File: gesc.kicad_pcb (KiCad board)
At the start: 4 copper layers, 111 x 111 mm, 150 parts, among them J1 Conn_01x06, J10 PHASE_C, J11 PHASE_B, J12 NTC, J13 T-Motor, J14 Conn_01x03, J15 EXT_OFF, J2 Conn_01x06, J3 Conn_01x06, J4 Conn_01x05, J5 Conn_01x03, J6 USB_B_Mini, J7 BAT+, J8 BAT-, J9 PHASE_A, Q1 TPH2R608NH,L1Q, Q2 TPH2R608NH,L1Q, Q3 TPH2R608NH,L1Q, Q4 TPH2R608NH,L1Q, Q5 TPH2R608NH,L1Q, Q6 TPH2R608NH,L1Q, U1 STM32F405RGTx, U10 LM5008MM, U11 SN74LVC1G66DBVR, U12 LM5107, U13 SN74LVC1G66DBVR, U14 TPS5430DDA, U15 LM5107, U16 EYSGJNZWY, U18 AQY282S, U2 SN74LVC1G66DBVR, U3 LM5107, U4 INA240A2, U5 INA240A2, U6 INA240A2, U7 SN74LVC1G66DBVR, U8 SN74LVC1G66DBVR, U9 SN74LVC1G66DBVR, Y1 X50328MSB2GI

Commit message: save
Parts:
- removed D10, D9: SMMBD914LT3G, Package_TO_SOT_SMD:SOT-23
- removed U18: AQY282S, Package_SO:SO-4_4.4x4.3mm_P2.54mm
- added C50: 22u/25V, Capacitor_SMD:C_0805_2012Metric, F.Cu at (175.5, 30.6)
- added C51: 10u0/75V, Capacitor_SMD:C_1210_3225Metric, F.Cu at (149.3, 31.2)
- added C52: 10u0/75V, Capacitor_SMD:C_1210_3225Metric, F.Cu at (149.3, 35.4)
- added C53: 10u0/75V, Capacitor_SMD:C_1210_3225Metric, F.Cu at (154.9, 31.2)
- added C55: 10u0/75V, Capacitor_SMD:C_1210_3225Metric, F.Cu at (154.9, 35.4)
- added C57: 10u0/75V, Capacitor_SMD:C_1210_3225Metric, F.Cu at (160.5, 31.2)
- added C58: 10u0/75V, Capacitor_SMD:C_1210_3225Metric, F.Cu at (160.5, 35.4)
- added D7: PMLL4153, Diode_SMD:D_MiniMELF, F.Cu at (170.1, 30.7)
- added R44: 34k0, Resistor_SMD:R_0805_2012Metric, F.Cu at (174.9, 33.8)
- added U17: LMR12010YMKE_NOPB, gesc:SOT95P280X110-6N, F.Cu at (88.0, 161.5)
- C19: value 100n -> 1u00
- C20, C31: value 10n0 -> 100n
- C23: value 10n0 -> 2n20
- C28: value 10u0/25V -> 22u/25V
- C33: value 100u -> 100n; footprint Capacitor_Tantalum_SMD:CP_EIA-3528-21_Kemet-B -> Capacitor_SMD:C_0805_2012Metric
- C34: value 100u -> 22u/25V; footprint Capacitor_Tantalum_SMD:CP_EIA-3528-21_Kemet-B -> Capacitor_SMD:C_0805_2012Metric
- D4: value SS210 -> SS110
- D5: value SS210 -> PMLL4153,115; footprint Diode_SMD:D_SMA -> Diode_SMD:D_MiniMELF
- D6: value B5819W -> SS110; footprint Diode_SMD:D_SOD-123 -> Diode_SMD:D_SMA
- D8: value SMMBD914LT3G -> SS110; footprint Package_TO_SOT_SMD:SOT-23 -> Diode_SMD:D_SMA
- J10, J11, J7, J8, J9: footprint gsvesc:TestPoint_Pad_5.0x5.0mm -> gesc:TestPoint_Pad_5.0x5.0mm
- J12: footprint gsvesc:2pad_smd_testpin -> gesc:2pad_smd_testpin
- L1: value 470u -> 330u; footprint Inductor_SMD:L_12x12mm_H6mm -> Inductor_SMD:L_12x12mm_H4.5mm
- L2: value 15u0 -> 4u70; footprint Inductor_SMD:L_7.3x7.3_H4.5 -> Inductor_SMD:L_Wuerth_WE-PD2-Typ-L
- Q1, Q2, Q3, Q4, Q5, Q6: footprint gsvesc:TRANS_TPHR8504PL-3PIN -> gesc:TRANS_TPHR8504PL-3PIN
- R12: value 680k -> 220k
- R15: value 680k -> 100k
- R16: value 10k0 -> 11k0
- R27: value 13k0 -> 10k0
- R34: value 7k50 -> 11k0
- U11, U13, U2, U7, U8, U9: footprint gsvesc:M74VHC1GT66DTT1G -> gesc:M74VHC1GT66DTT1G
- U14: value TPS5430DDA -> AQY282S; footprint Package_SO:TI_SO-PowerPAD-8_ThermalVias -> Package_SO:SO-4_4.4x4.3mm_P2.54mm
- U16: footprint gsvesc:BLE_EYSGJNZWY -> gesc:BLE_EYSGJNZWY
- U4, U5, U6: footprint gsvesc:INA240A1QPWRQ1 -> gesc:INA240A1QPWRQ1
- moved D8 73.2 mm to (66.8, 151.6)
- moved U14 30.7 mm to (126.0, 142.5), turned to 180 degrees
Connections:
- C17 pad 2: GND -> Net-(C17-Pad2)
- C31 pad 1: Net-(C31-Pad1) -> Net-(C17-Pad2)
- C31 pad 2: Net-(C31-Pad2) -> GND
- C33 pad 1: VCC -> Net-(C33-Pad1)
- C33 pad 2: GND -> Net-(C33-Pad2)
- D5 pad 1: Net-(C31-Pad1) -> Net-(C19-Pad1)
- D5 pad 2: GND -> +12V
- D6 pad 1: Net-(C19-Pad1) -> +12V
- D6 pad 2: +12V -> VBUS
- D8 pad 1: +12V -> Net-(C33-Pad2)
- D8 pad 2: (no net) -> GND
- J6 pad 1: (no net) -> VBUS
- L2 pad 2: Net-(C31-Pad1) -> Net-(C33-Pad2)
- R27 pad 1: VCC -> +12V
- R34 pad 1: Net-(R27-Pad2) -> GND
- R34 pad 2: GND -> Net-(R34-Pad2)
- U14 pad 1: Net-(C31-Pad2) -> /Driver/EN_3V3
- U14 pad 2: (no net) -> GND
- U14 pad 3: (no net) -> GND
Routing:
- net Net-(U14-Pad5): track 26.1 -> 0.00 mm, vias 2 -> 0
- net Net-(R27-Pad2): track 5.96 -> 32.1 mm, vias 0 -> 2
- net VCC: track 96.3 -> 89.1 mm
- net +12V: track 174.3 -> 181.5 mm
- net Net-(C31-Pad2): track 2.90 -> 0.00 mm
- net GND: track 20.2 -> 21.8 mm, vias 351 -> 350
- net Net-(C17-Pad2): track 0.00 -> 1.29 mm, vias 0 -> 1
- added copper zone on F.Cu, net Net-(C17-Pad2)
- removed copper zone on F.Cu, net Net-(C31-Pad1)

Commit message: save
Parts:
- moved D6 14.7 mm to (108.8, 163.2)

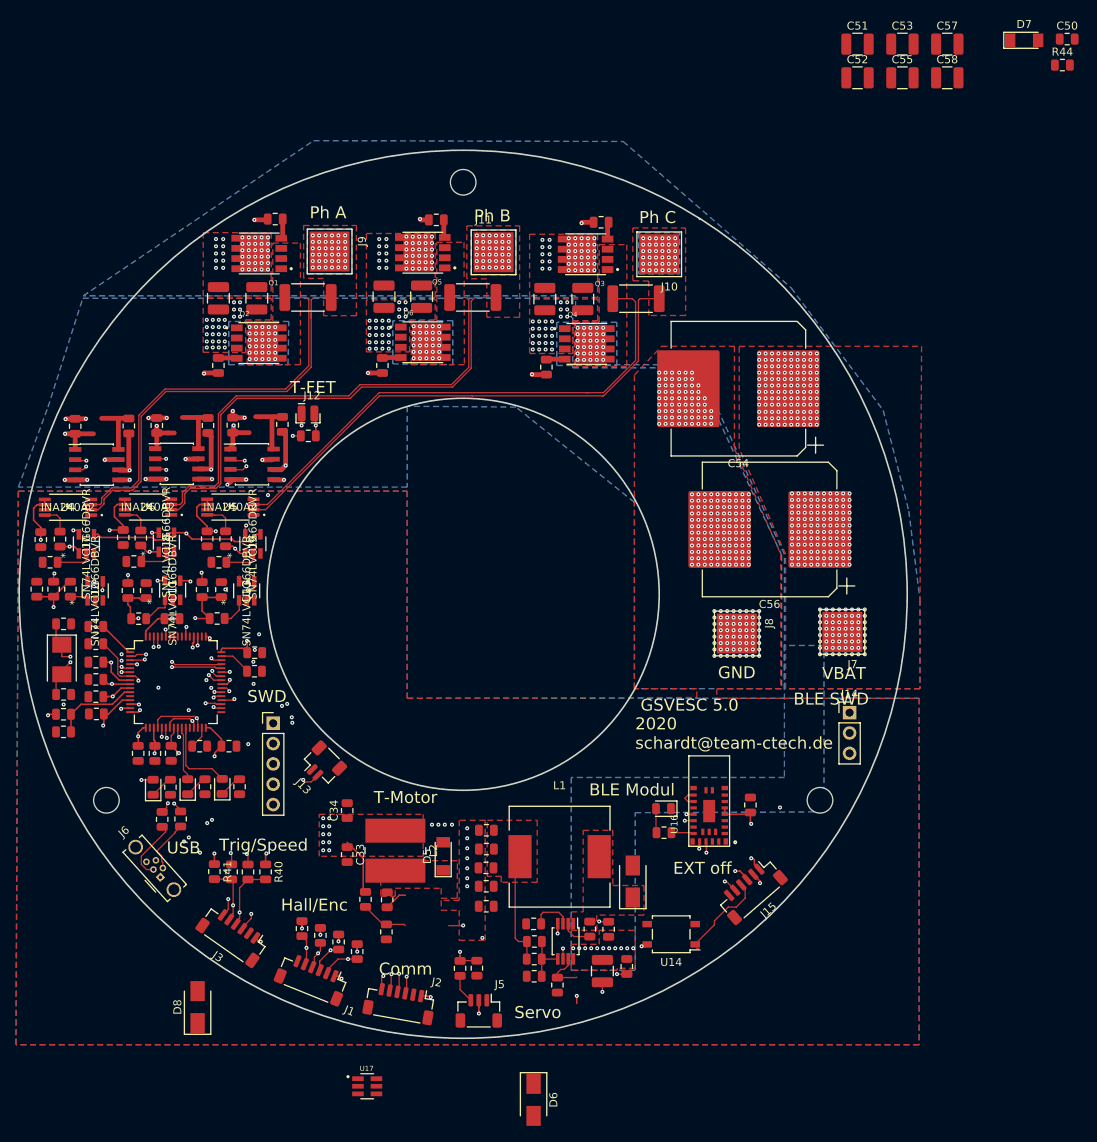
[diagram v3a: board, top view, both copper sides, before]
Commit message: PCB updated: - reroute SH_X - change 3V3 Power supply - add VBUS to 3V3 regulator - use LM5107 - change Layer/Plane assignment - move current sense tracks to layer 2
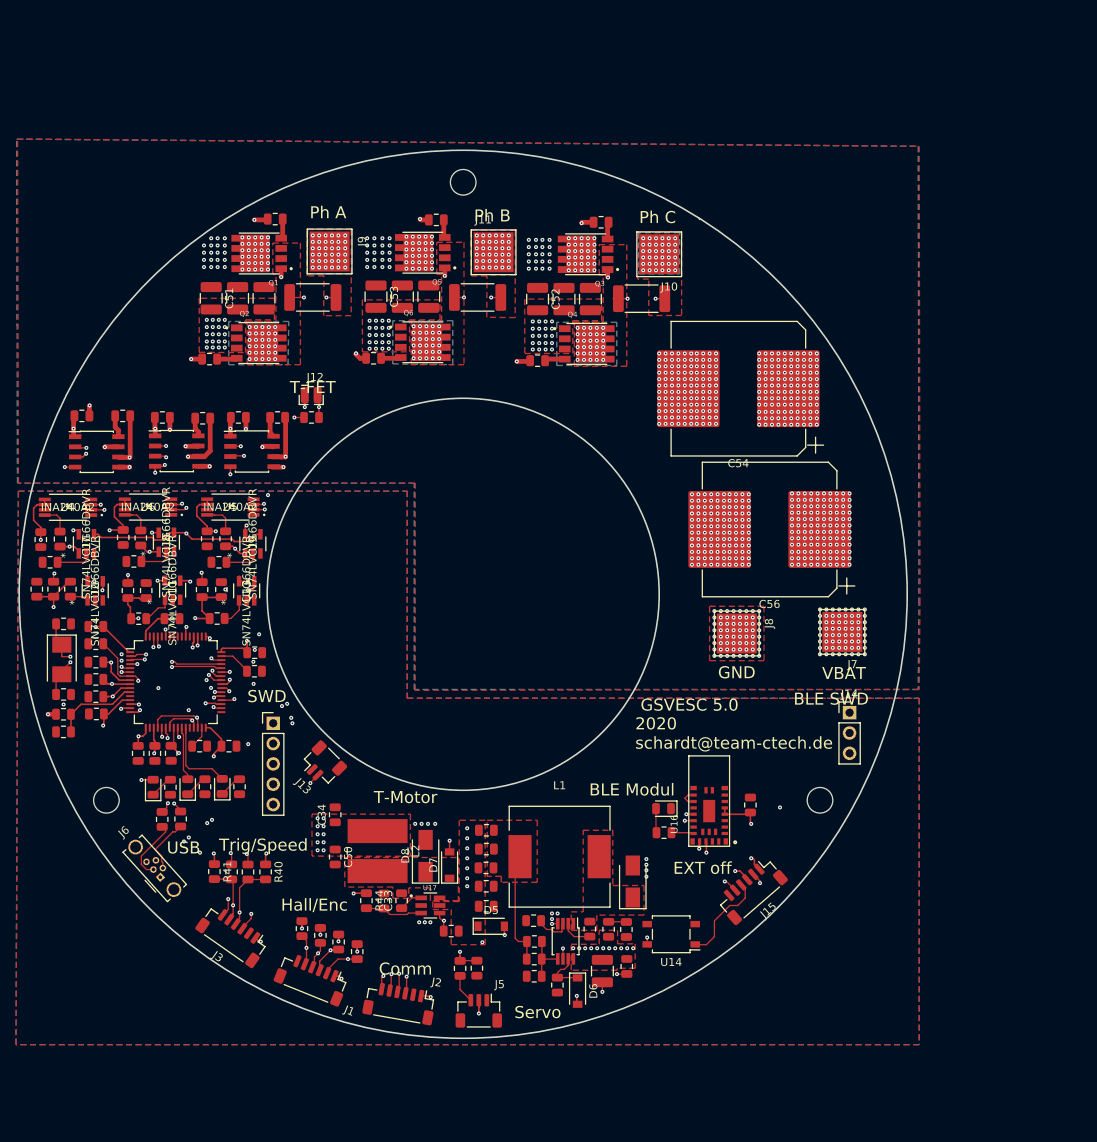
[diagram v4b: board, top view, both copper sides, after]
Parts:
- removed C55, C57, C58: 10u0/75V, Capacitor_SMD:C_1210_3225Metric
- removed the D5 at (97.5, 132.7)
- added D6: B5819W, Diode_SMD:D_SOD-123, F.Cu at (114.3, 149.6)
- D5: renamed from D6; value SS110 -> B5819W; footprint Diode_SMD:D_SMA -> Diode_SMD:D_SOD-123
- D7: value PMLL4153 -> B5819W; footprint Diode_SMD:D_MiniMELF -> Diode_SMD:D_SOD-123
- moved C50 137.2 mm to (84.0, 132.8), turned to 270 degrees
- moved R44 135.9 mm to (87.9, 138.3), turned to 270 degrees
- moved D7 125.6 mm to (98.3, 133.8), turned to 90 degrees
- moved C51 86.8 mm to (68.5, 63.0), turned to 270 degrees
- moved C53 73.0 mm to (89.1, 62.8), turned to 270 degrees
- moved C52 48.6 mm to (109.3, 63.1), turned to 270 degrees
- moved D8 34.2 mm to (95.3, 132.7)
- moved C31 30.1 mm to (120.4, 141.9)
- moved U17 23.9 mm to (95.9, 138.9)
- moved D5 22.3 mm to (103.5, 141.5), turned to 0 degrees
- moved R27 11.4 mm to (98.5, 142.1), turned to 180 degrees
- moved C33 8.91 mm to (92.3, 138.3), turned to 90 degrees
- moved R34 3.87 mm to (90.1, 138.3)
- moved C36 2.40 mm to (112.6, 63.1)
- moved C39 2.40 mm to (71.8, 63.0)
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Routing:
- net VBUS: track 0.00 -> 47.2 mm, vias 0 -> 1
- net +12V: track 181.5 -> 164.1 mm
- net /Driver/SH_C: track 135.5 -> 145.7 mm, vias 32 -> 35
- net GND: track 21.8 -> 11.7 mm, vias 350 -> 388
- net /Driver/SH_A: track 103.9 -> 111.6 mm, vias 32 -> 35
- net Net-(R34-Pad2): track 0.00 -> 7.24 mm
- net /Driver/SH_B: track 124.1 -> 130.0 mm, vias 32 -> 35
- net Net-(C32-Pad1): track 7.63 -> 2.53 mm
- net /Driver/GL_B: track 28.5 -> 33.5 mm
- net VCC: track 89.1 -> 93.9 mm, vias 40 -> 42
- net Net-(C27-Pad1): track 7.16 -> 2.36 mm
- net Net-(C21-Pad1): track 7.31 -> 2.76 mm
- net /Driver/GH_C: track 61.4 -> 57.1 mm
- net /POWER/PHASE_B: track 62.4 -> 58.3 mm, vias 36 -> 38
- net /POWER/PHASE_A: track 51.2 -> 47.8 mm, vias 36 -> 38
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- added copper zone on F.Cu, net Net-(C33-Pad2)
- added copper zone on In2.Cu, net VCC
- removed copper zone on In2.Cu, net GND
- removed copper zone on F.Cu, net Net-(C17-Pad2)
- removed copper zone on B.Cu, net VBAT
- removed copper zone on In1.Cu, net VBAT
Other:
- net class Default: clearance 0.15 -> 0.2
- rule trace_clearance: 0.15 -> 0.2

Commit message: - remove solder-mask from bottom layer
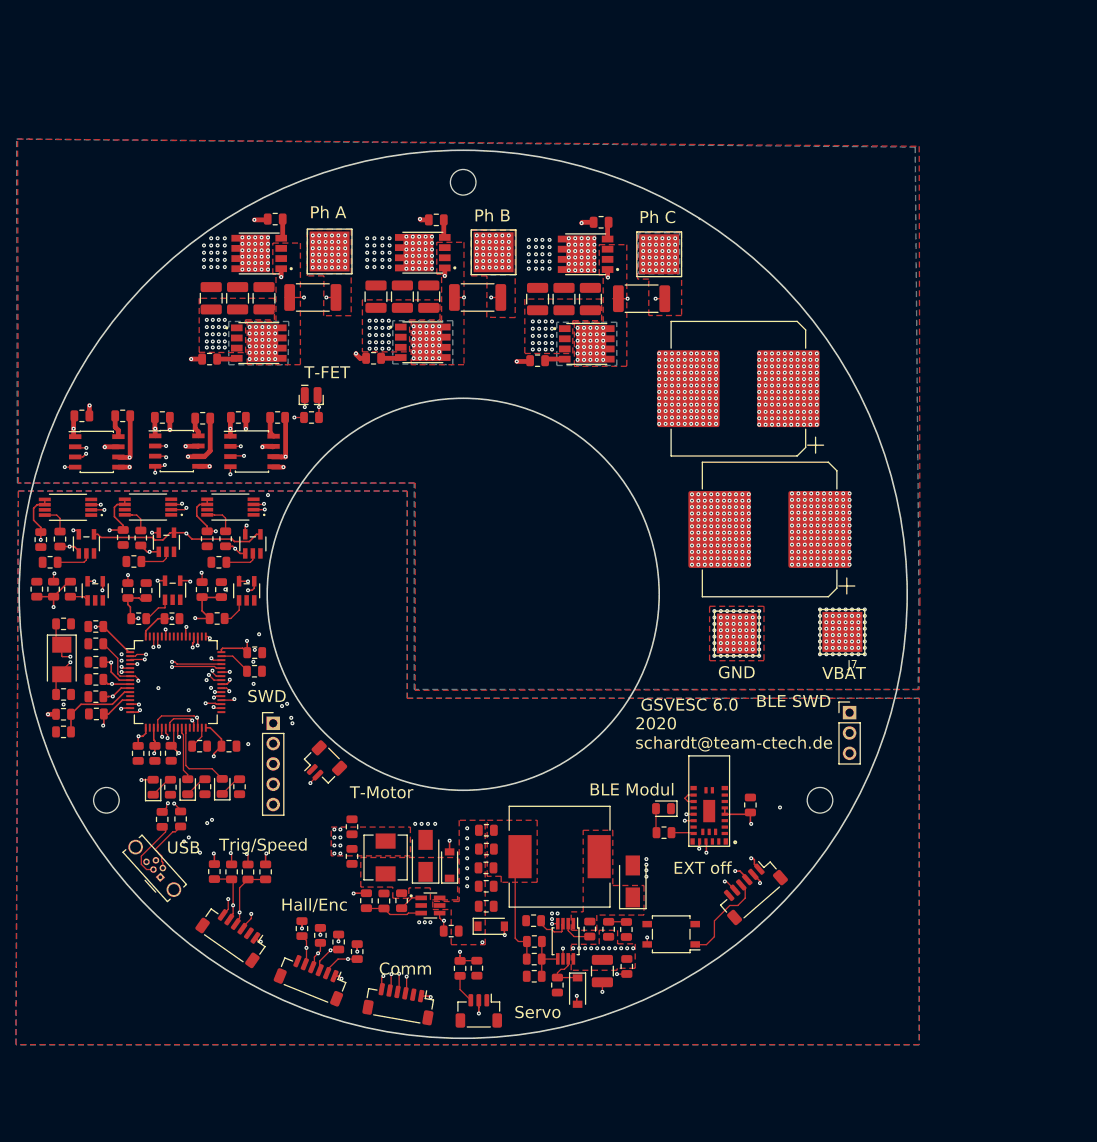
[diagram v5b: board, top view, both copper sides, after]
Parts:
- C19: value 1u00 -> 100n
- C23: value 2n20 -> 1n00
- C28, C34, C50: value 22u/25V -> 22u0/25V
- D4, D8: value SS110 -> SS210
- L2: footprint Inductor_SMD:L_Wuerth_WE-PD2-Typ-L -> Inductor_SMD:L_Sunlord_MWSA0518_5.4x5.2mm
- R1, R37: value 0R00 -> 0r00
- R10, R11: value 221R -> 221r
- R2, R3: value 22R1 -> 10r0
- R24, R38, R39: value 4R75 -> 4r75
- R25, R26, R28, R32, R42, R43: value 4R75 -> 10r0
- R27, R36, R8: value 10k0 -> 11k0
- R31, R45, R46: value 0R0005 -> 0r001
- R40, R41: value 10K0 -> 11k0
- R44: value 34k0 -> 33k0
- R5: value 100R -> 10r0
- U4, U5, U6: value INA240A2 -> INA240A1
- moved C34 2.58 mm to (86.1, 129.1)
- moved C50 2.10 mm to (86.1, 132.8)
- moved L2 1.28 mm to (90.3, 132.9)
- renumbered U8 to e
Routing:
- net VCC: vias 42 -> 40
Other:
- net class Default: clearance 0.2 -> 0.15
- net class GATES: clearance 0.2 -> 0
- rule trace_clearance: 0.2 -> 0.15
- board text added: "GSVESC 6.0"
- board text removed: "GSVESC 5.0"

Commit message: - add separate connection between lowside source and driver
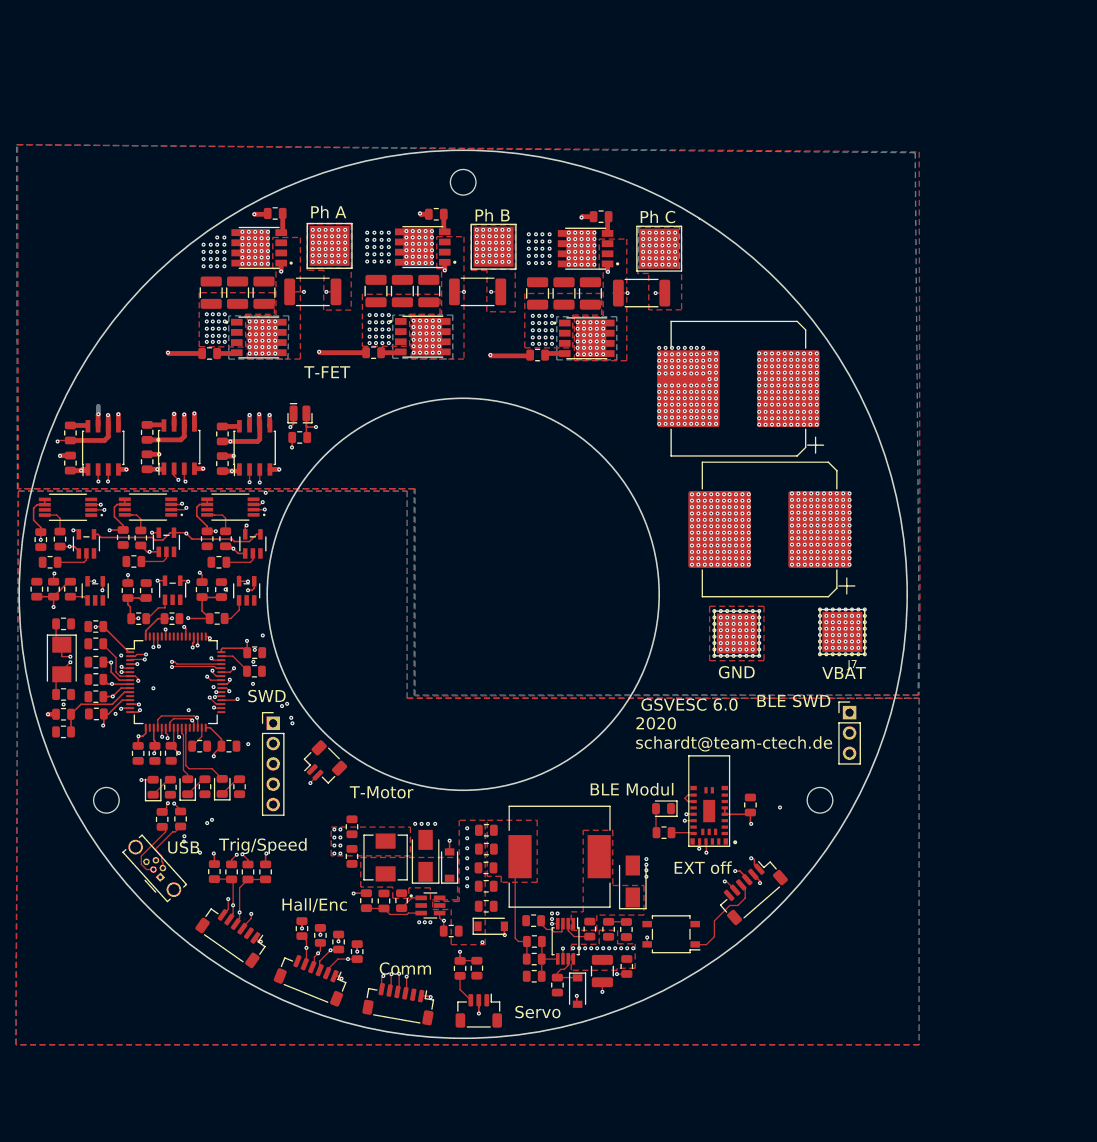
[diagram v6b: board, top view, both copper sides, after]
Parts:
- moved C32 7.20 mm to (69.9, 80.0), turned to 270 degrees
- moved C27 7.16 mm to (60.5, 79.8), turned to 270 degrees
- moved C21 6.88 mm to (50.9, 79.8), turned to 270 degrees
- moved C29 6.10 mm to (69.9, 83.7), turned to 90 degrees
- moved C15 6.07 mm to (50.9, 83.6), turned to 90 degrees
- moved C22 5.85 mm to (60.5, 83.4), turned to 90 degrees
- moved R36 2.90 mm to (79.6, 80.4)
- moved J12 2.69 mm to (79.6, 76.2)
- moved U3 0.94 mm to (55.0, 81.7), turned to 90 degrees
- moved C36 0.70 mm to (112.6, 62.4)
- moved C37 0.70 mm to (75.1, 62.3)
- moved C39 0.70 mm to (71.8, 62.3)
- moved C43 0.70 mm to (115.9, 62.4)
- moved C51 0.70 mm to (68.5, 62.3)
- moved C52 0.70 mm to (109.3, 62.4)
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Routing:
- net GND: track 11.7 -> 114.2 mm, vias 388 -> 387
- net /Driver/GL_B: track 33.5 -> 27.5 mm
- net /Driver/GL_A: track 21.4 -> 16.1 mm
- net +12V: track 164.1 -> 158.7 mm
- net /MCU/H2: track 34.0 -> 29.2 mm
- net /MCU/H1: track 42.9 -> 38.2 mm
- net /MCU/H3: track 31.4 -> 27.4 mm
- net /MCU/L2: track 36.3 -> 32.7 mm
- net VCC: track 93.9 -> 90.9 mm
- net /Driver/GH_A: track 41.0 -> 38.0 mm
- net /MCU/SERVO: track 69.2 -> 66.3 mm
- net /MCU/L3: track 34.6 -> 31.9 mm
- net /Driver/SH_A: track 111.6 -> 109.0 mm, vias 35 -> 36
- net /Driver/GH_B: track 50.6 -> 48.3 mm
- net /POWER/PHASE_B: track 58.3 -> 60.4 mm
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
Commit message: JLC ready
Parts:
- Q1, Q2, Q3, Q4, Q5, Q6: value TPH2R608NH,L1Q -> BSC070N10NS5; footprint gesc:TRANS_TPHR8504PL-3PIN -> Package_TO_SOT_SMD:TDSON-8-1
- moved R42 0.50 mm to (96.1, 52.5)
- moved Q4 0.20 mm to (115.2, 68.0)
- moved Q5 0.20 mm to (95.1, 56.6)
- moved Q1 0.15 mm to (74.6, 56.7)
- moved Q6 0.15 mm to (94.8, 67.8)
- moved Q3 0.11 mm to (115.4, 56.8)
- moved Q2 0.10 mm to (74.3, 67.9)
- renumbered e to U8
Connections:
- Q1 pad 1: VBAT -> /Driver/SH_A
- Q1 pad 2: Net-(Q1-Pad2) -> /Driver/SH_A
- Q2 pad 1: /Driver/SH_A -> GND
- Q2 pad 2: Net-(Q2-Pad2) -> GND
- Q3 pad 1: VBAT -> /Driver/SH_C
- Q3 pad 2: Net-(Q3-Pad2) -> /Driver/SH_C
- Q4 pad 1: /Driver/SH_C -> GND
- Q4 pad 2: Net-(Q4-Pad2) -> GND
- Q5 pad 1: VBAT -> /Driver/SH_B
- Q5 pad 2: Net-(Q5-Pad2) -> /Driver/SH_B
- Q6 pad 1: /Driver/SH_B -> GND
- Q6 pad 2: Net-(Q6-Pad2) -> GND
- R25 pad 1: Net-(Q3-Pad2) -> Net-(Q3-Pad4)
- R26 pad 1: Net-(Q4-Pad2) -> Net-(Q4-Pad4)
- R28 pad 1: Net-(Q1-Pad2) -> Net-(Q1-Pad4)
- R32 pad 1: Net-(Q2-Pad2) -> Net-(Q2-Pad4)
- R42 pad 1: Net-(Q5-Pad2) -> Net-(Q5-Pad4)
- R43 pad 1: Net-(Q6-Pad2) -> Net-(Q6-Pad4)
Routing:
- net /Driver/SH_B: track 129.0 -> 138.1 mm
- net /Driver/SH_A: track 109.0 -> 117.7 mm
- net /Driver/SH_C: track 146.5 -> 154.4 mm
- net GND: track 114.2 -> 120.5 mm
- net Net-(Q5-Pad4): track 0.00 -> 3.02 mm
- net Net-(Q4-Pad4): track 0.00 -> 2.65 mm
- net Net-(Q4-Pad2): track 2.65 -> 0.00 mm
- net Net-(Q2-Pad4): track 0.00 -> 2.56 mm
- net Net-(Q2-Pad2): track 2.56 -> 0.00 mm
- net Net-(Q6-Pad4): track 0.00 -> 2.50 mm
- net Net-(Q6-Pad2): track 2.50 -> 0.00 mm
- net Net-(Q1-Pad4): track 0.00 -> 2.21 mm
- net Net-(Q1-Pad2): track 2.21 -> 0.00 mm
- net Net-(Q3-Pad4): track 0.00 -> 2.15 mm
- net Net-(Q3-Pad2): track 2.15 -> 0.00 mm
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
